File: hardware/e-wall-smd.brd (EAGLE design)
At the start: 50.8 x 48.3 mm, 70 parts, among them IC1 74HCT595D, IC2 74HCT595D, IC3 74HCT595D, IC4 74HCT595D, Q1 SI2302CDS, Q10 SI2302CDS, Q11 SI2302CDS, Q12 SI2302CDS, Q13 SI2302CDS, Q14 SI2302CDS, Q15 SI2302CDS, Q16 SI2302CDS, Q17 SI2302CDS, Q18 SI2302CDS, Q19 SI2302CDS, Q2 SI2302CDS, Q20 SI2302CDS, Q21 SI2302CDS, Q22 SI2302CDS, Q23 SI2302CDS, Q24 SI2302CDS, Q25 SI4214DDY, Q26 SI4214DDY, Q27 SI4214DDY, Q28 SI4214DDY, Q29 SI2302CDS, Q3 SI2302CDS, Q30 SI2302CDS, Q31 SI2347DS, Q4 SI2302CDS, Q5 SI2302CDS, Q6 SI2302CDS, Q7 SI2302CDS, Q8 SI2302CDS, Q9 SI2302CDS

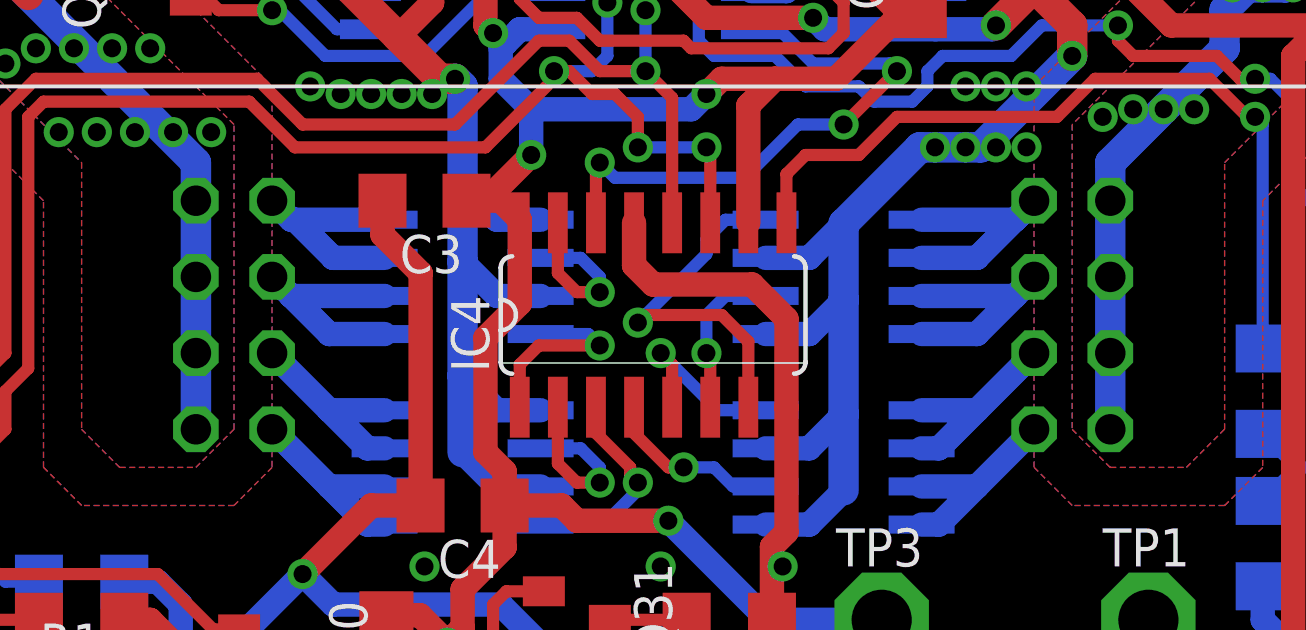
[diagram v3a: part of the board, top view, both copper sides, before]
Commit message: Freilaufdioden bei Hochstromausgängen
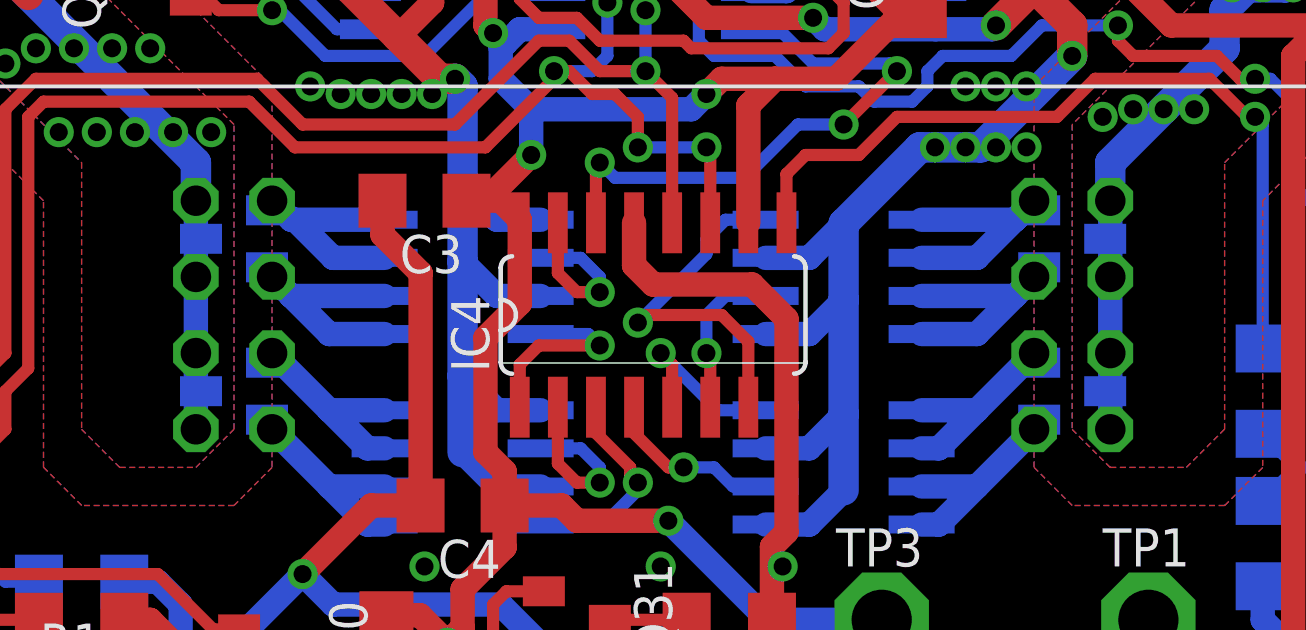
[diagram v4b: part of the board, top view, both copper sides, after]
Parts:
- added D13, D14, D15, D16: BAS40-05, diode:SOT23
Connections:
- net +12V: now also D13.3, D14.3, D15.3, D16.3
- net OUT24: now also D13.1
- net OUT25: now also D13.2
- net OUT26: now also D14.1
- net OUT27: now also D14.2
- net OUT28: now also D15.1
- net OUT29: now also D15.2
- net OUT30: now also D16.1
- net OUT31: now also D16.2
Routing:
- net +12V: track 143.8 -> 144.4 mm
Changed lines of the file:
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@@
 <element name="C3" library="resistor" package="C1206" value="33n" x="17.78" y="19.05" rot="R180"/>
 <element name="C4" library="resistor" package="C1206" value="33n" x="19.05" y="8.89" rot="R180"/>
+<element name="D13" library="diode" package="SOT23" value="BAS40-05" x="11.43" y="17.78" rot="MR270"/>
+<element name="D14" library="diode" package="SOT23" value="BAS40-05" x="11.43" y="12.7" rot="MR270"/>
+<element name="D15" library="diode" package="SOT23" value="BAS40-05" x="39.37" y="12.7" rot="MR90"/>
+<element name="D16" library="diode" package="SOT23" value="BAS40-05" x="39.37" y="17.78" rot="MR90"/>
 </elements>
 <signals>
@@
 <contactref element="SV5" pad="3"/>
 <contactref element="SV5" pad="1"/>
-<wire x1="10.16" y1="11.43" x2="10.16" y2="13.97" width="1.016" layer="16"/>
-<wire x1="10.16" y1="13.97" x2="10.16" y2="16.51" width="1.016" layer="16"/>
-<wire x1="10.16" y1="16.51" x2="10.16" y2="19.05" width="1.016" layer="16"/>
 <wire x1="10.16" y1="19.05" x2="10.16" y2="20.32" width="1.016" layer="16"/>
 <wire x1="10.16" y1="20.32" x2="2.54" y2="27.94" width="1.016" layer="16"/>
@@
 <wire x1="45.212" y1="26.162" x2="46.482" y2="26.162" width="1.016" layer="16"/>
 <wire x1="46.482" y1="26.162" x2="48.26" y2="27.94" width="1.016" layer="16"/>
-<wire x1="40.64" y1="11.43" x2="40.64" y2="13.97" width="1.016" layer="16"/>
-<wire x1="40.64" y1="13.97" x2="40.64" y2="16.51" width="1.016" layer="16"/>
-<wire x1="40.64" y1="16.51" x2="40.64" y2="19.05" width="1.016" layer="16"/>
 <contactref element="TP2" pad="TP"/>
 <wire x1="12.7" y1="44.45" x2="12.7" y2="47.244" width="1.016" layer="1"/>
@@
 <via x="45.72" y="26.162" extent="1-16" drill="0.6"/>
 <via x="44.704" y="26.162" extent="1-16" drill="0.6"/>
+<contactref element="D13" pad="3"/>
+<contactref element="D14" pad="3"/>
+<contactref element="D15" pad="3"/>
+<contactref element="D16" pad="3"/>
+<wire x1="10.33" y1="17.78" x2="10.16" y2="17.95" width="0.8128" layer="16"/>
+<wire x1="10.16" y1="17.95" x2="10.16" y2="19.05" width="0.8128" layer="16"/>
+<wire x1="10.33" y1="17.78" x2="10.16" y2="17.61" width="0.8128" layer="16"/>
+<wire x1="10.16" y1="17.61" x2="10.16" y2="16.51" width="0.8128" layer="16"/>
+<wire x1="10.33" y1="12.7" x2="10.16" y2="12.87" width="0.8128" layer="16"/>
+<wire x1="10.16" y1="12.87" x2="10.16" y2="13.97" width="0.8128" layer="16"/>
+<wire x1="10.33" y1="12.7" x2="10.16" y2="12.53" width="0.8128" layer="16"/>
+<wire x1="10.16" y1="12.53" x2="10.16" y2="11.43" width="0.8128" layer="16"/>
+<wire x1="10.16" y1="13.97" x2="10.16" y2="16.51" width="0.8128" layer="16"/>
+<wire x1="40.47" y1="12.7" x2="40.64" y2="12.53" width="0.8128" layer="16"/>
+<wire x1="40.64" y1="12.53" x2="40.64" y2="11.43" width="0.8128" layer="16"/>
+<wire x1="40.47" y1="12.7" x2="40.64" y2="12.87" width="0.8128" layer="16"/>
+<wire x1="40.64" y1="12.87" x2="40.64" y2="13.97" width="0.8128" layer="16"/>
+<wire x1="40.64" y1="13.97" x2="40.64" y2="16.51" width="0.8128" layer="16"/>
+<wire x1="40.47" y1="17.78" x2="40.64" y2="17.61" width="0.8128" layer="16"/>
+<wire x1="40.64" y1="17.61" x2="40.64" y2="16.51" width="0.8128" layer="16"/>
+<wire x1="40.47" y1="17.78" x2="40.64" y2="17.95" width="0.8128" layer="16"/>
+<wire x1="40.64" y1="17.95" x2="40.64" y2="19.05" width="0.8128" layer="16"/>
 </signal>
 <signal name="SOMI_UC">
@@
 <wire x1="16.45" y1="17.145" x2="14.732" y2="17.145" width="0.8128" layer="16"/>
 <wire x1="14.732" y1="17.145" x2="13.462" y2="18.415" width="0.8128" layer="16"/>
+<contactref element="D13" pad="1"/>
+<wire x1="12.53" y1="18.73" x2="12.7" y2="18.9" width="0.8128" layer="16"/>
+<wire x1="12.7" y1="18.9" x2="12.7" y2="19.05" width="0.8128" layer="16"/>
 </signal>
 <signal name="OUT25">
@@
 <wire x1="16.45" y1="14.605" x2="14.605" y2="14.605" width="0.8128" layer="16"/>
 <wire x1="14.605" y1="14.605" x2="13.335" y2="15.875" width="0.8128" layer="16"/>
+<contactref element="D13" pad="2"/>
+<wire x1="12.53" y1="16.83" x2="12.7" y2="16.66" width="0.8128" layer="16"/>
+<wire x1="12.7" y1="16.66" x2="12.7" y2="16.51" width="0.8128" layer="16"/>
 </signal>
 <signal name="OUT26">
@@
 <wire x1="16.45" y1="10.795" x2="15.875" y2="10.795" width="0.8128" layer="16"/>
 <wire x1="15.875" y1="10.795" x2="14.605" y2="12.065" width="0.8128" layer="16"/>
+<contactref element="D14" pad="1"/>
+<wire x1="12.53" y1="13.65" x2="12.7" y2="13.82" width="0.8128" layer="16"/>
+<wire x1="12.7" y1="13.82" x2="12.7" y2="13.97" width="0.8128" layer="16"/>
 </signal>
 <signal name="OUT27">
@@
 <wire x1="16.45" y1="8.255" x2="15.875" y2="8.255" width="0.8128" layer="16"/>
 <wire x1="15.875" y1="8.255" x2="14.605" y2="9.525" width="0.8128" layer="16"/>
+<contactref element="D14" pad="2"/>
+<wire x1="12.53" y1="11.75" x2="12.7" y2="11.58" width="0.8128" layer="16"/>
+<wire x1="12.7" y1="11.58" x2="12.7" y2="11.43" width="0.8128" layer="16"/>
 </signal>
 <signal name="OUT28">
@@
 <wire x1="34.35" y1="8.255" x2="34.925" y2="8.255" width="0.8128" layer="16"/>
 <wire x1="34.925" y1="8.255" x2="36.195" y2="9.525" width="0.8128" layer="16"/>
+<contactref element="D15" pad="1"/>
+<wire x1="38.27" y1="11.75" x2="38.1" y2="11.58" width="0.8128" layer="16"/>
+<wire x1="38.1" y1="11.58" x2="38.1" y2="11.43" width="0.8128" layer="16"/>
 </signal>
 <signal name="OUT29">
@@
 <wire x1="34.35" y1="10.795" x2="34.925" y2="10.795" width="0.8128" layer="16"/>
 <wire x1="34.925" y1="10.795" x2="36.195" y2="12.065" width="0.8128" layer="16"/>
+<contactref element="D15" pad="2"/>
+<wire x1="38.27" y1="13.65" x2="38.1" y2="13.82" width="0.8128" layer="16"/>
+<wire x1="38.1" y1="13.82" x2="38.1" y2="13.97" width="0.8128" layer="16"/>
 </signal>
 <signal name="OUT30">
@@
 <contactref element="Q28" pad="7"/>
 <wire x1="34.35" y1="15.875" x2="37.465" y2="15.875" width="0.8128" layer="16"/>
-<wire x1="37.465" y1="15.875" x2="37.719" y2="16.129" width="0.8128" layer="16"/>
-<wire x1="37.719" y1="16.129" x2="38.1" y2="16.51" width="0.8128" layer="16"/>
+<wire x1="37.465" y1="15.875" x2="38.1" y2="16.51" width="0.8128" layer="16"/>
 <wire x1="34.35" y1="14.605" x2="36.195" y2="14.605" width="0.8128" layer="16"/>
 <wire x1="36.195" y1="14.605" x2="37.465" y2="15.875" width="0.8128" layer="16"/>
+<contactref element="D16" pad="1"/>
+<wire x1="38.27" y1="16.83" x2="38.1" y2="16.66" width="0.8128" layer="16"/>
+<wire x1="38.1" y1="16.66" x2="38.1" y2="16.51" width="0.8128" layer="16"/>
 </signal>
 <signal name="OUT31">
@@
 <wire x1="34.35" y1="17.145" x2="36.195" y2="17.145" width="0.8128" layer="16"/>
 <wire x1="36.195" y1="17.145" x2="38.1" y2="19.05" width="0.8128" layer="16"/>
+<contactref element="D16" pad="2"/>
+<wire x1="38.27" y1="18.73" x2="38.1" y2="18.9" width="0.8128" layer="16"/>
+<wire x1="38.1" y1="18.9" x2="38.1" y2="19.05" width="0.8128" layer="16"/>
 </signal>
 <signal name="+5V" class="1">

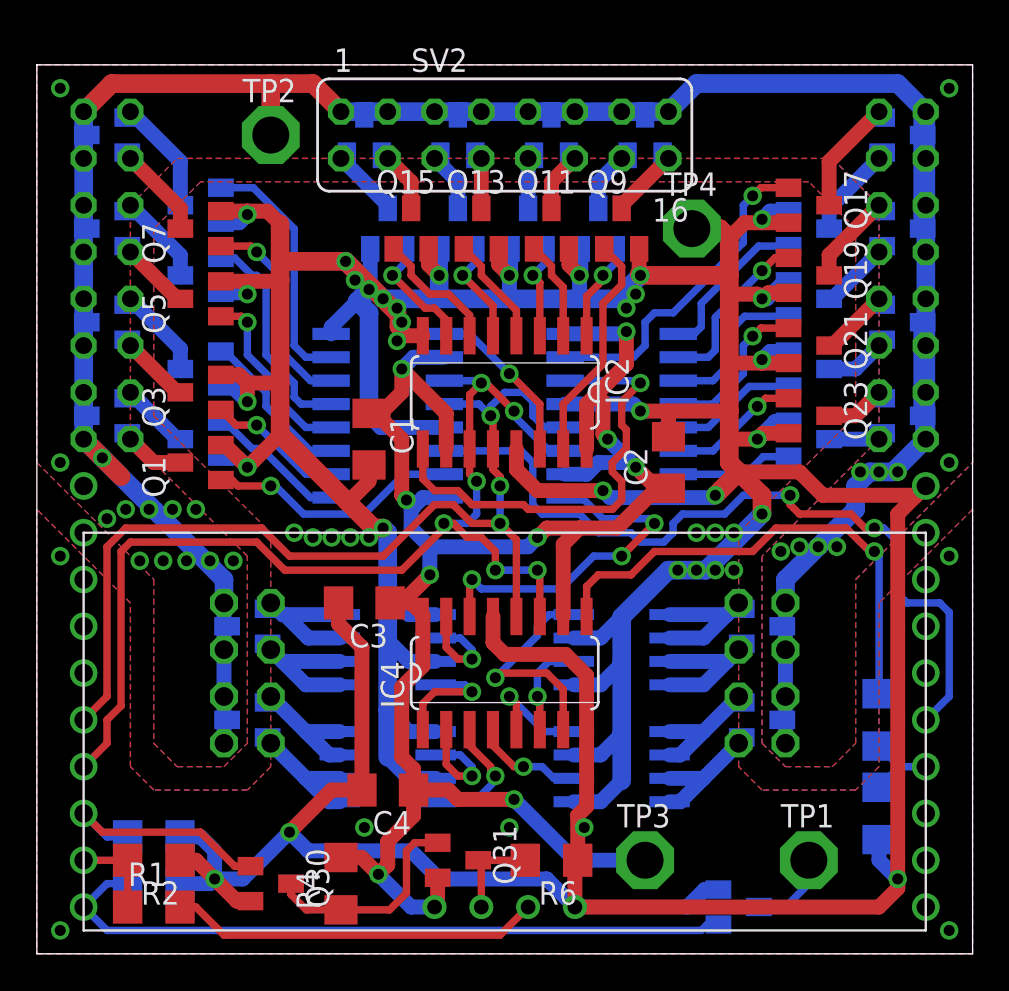
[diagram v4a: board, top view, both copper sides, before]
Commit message: Design Rules von Platinensammler angewendet
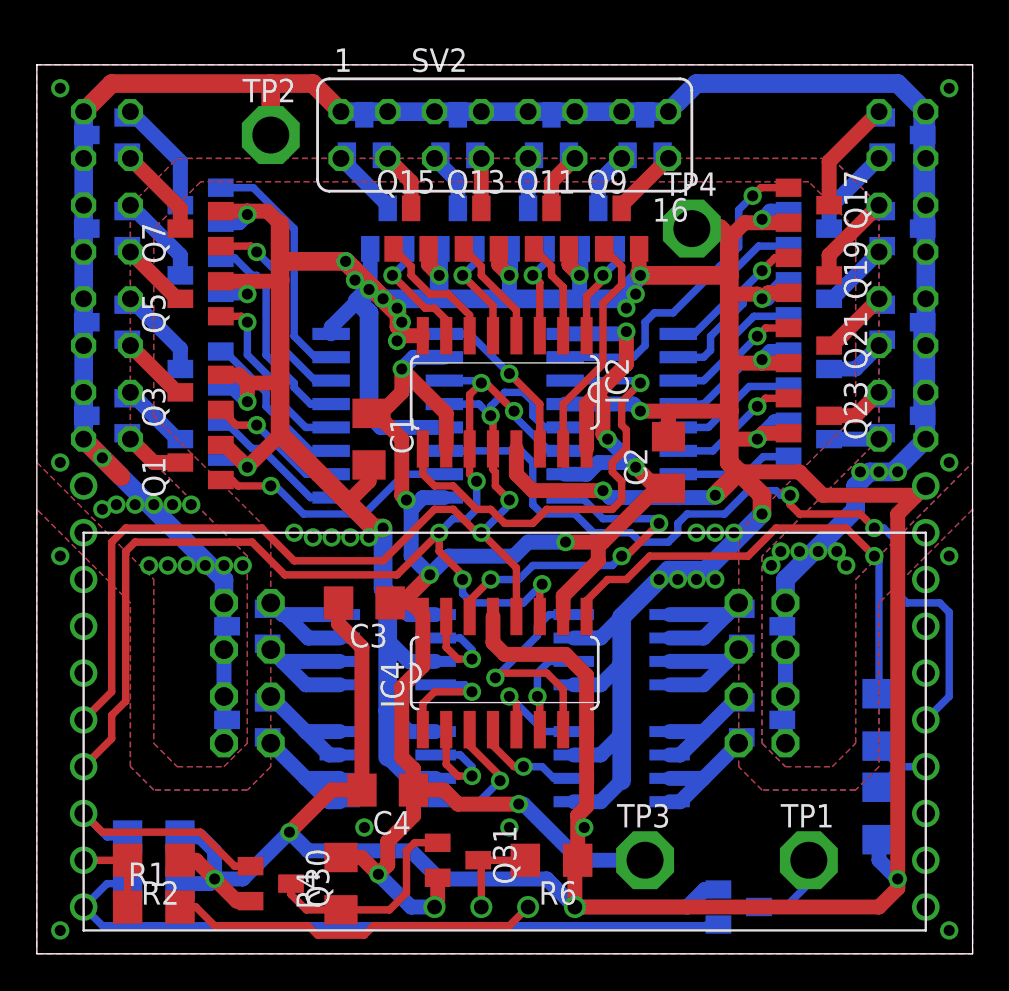
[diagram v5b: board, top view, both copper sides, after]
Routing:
- net CLK: track 59.2 -> 60.2 mm
- net SOMI: track 26.9 -> 26.3 mm
- net SIG19: track 8.48 -> 7.88 mm
- net N$3: track 19.1 -> 18.6 mm
- net +12V: vias 22 -> 26
